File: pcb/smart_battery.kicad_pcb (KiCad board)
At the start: 2 copper layers, 35 parts, among them J11 Conn_01x05_RTC, J12 Conn_HtrTh, J13 Conn_BattTh, Q1 MMBT5551L, Q2 MMBT5551L, U1 SPX3819M5-L-3-3, U10 FEATHER_M0_ADALOGGER, U11 FEATHERWING_HEATER_RELAY, U12 FEATHERWING_ETHERNET, U13 FEATHERWING_MINI_RELAY, U14 FEATHERWING_MINI_RELAY, U1Batt1 LTC4151CS-2PBF, U2Solar1 LTC4151CS-2PBF

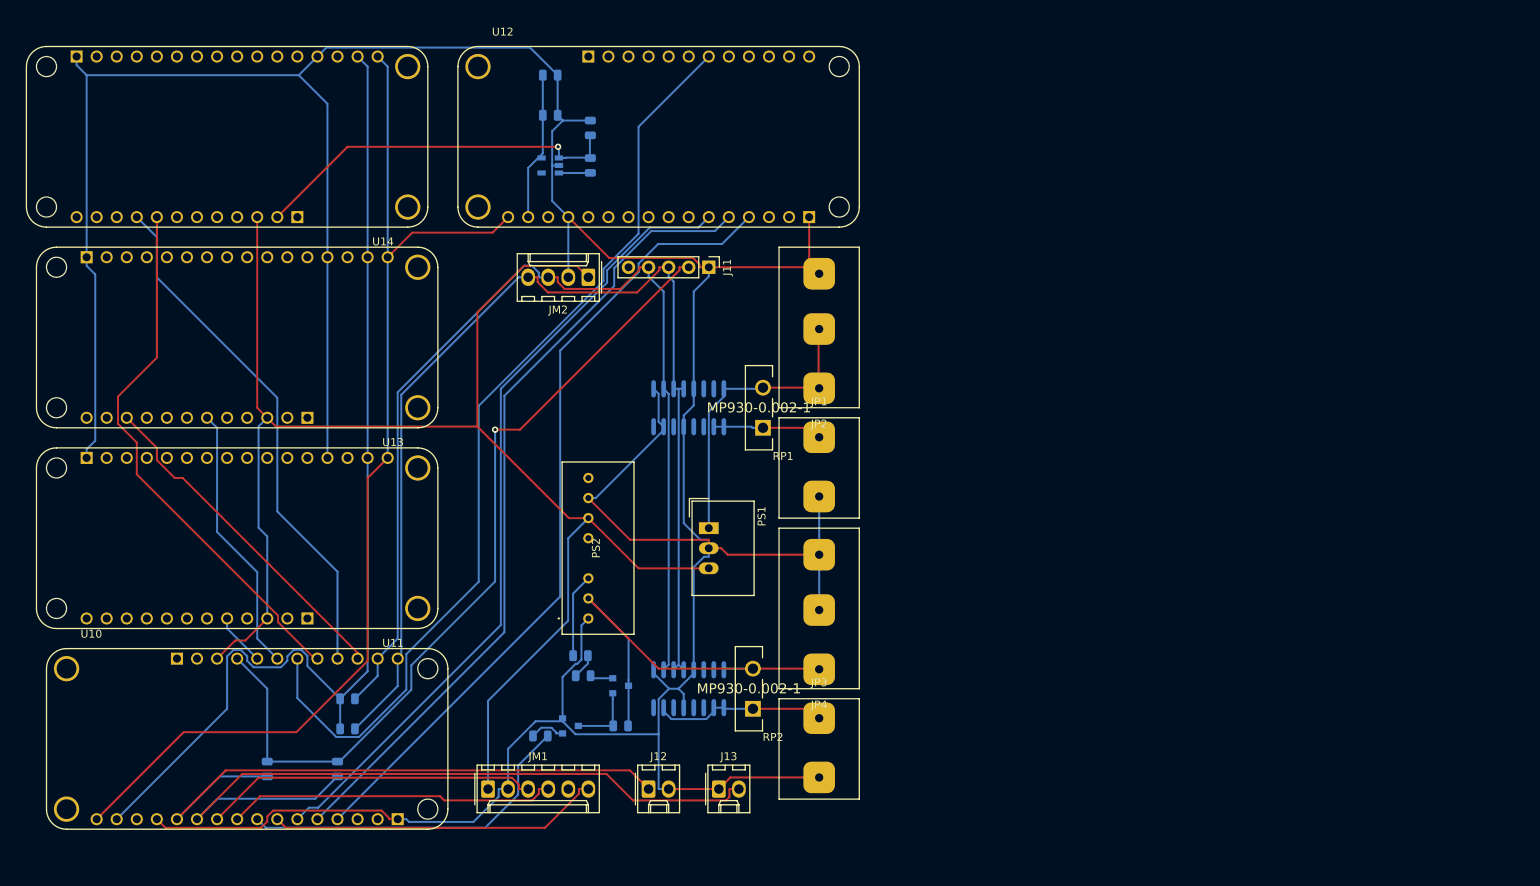
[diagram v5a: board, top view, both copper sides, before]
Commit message: Made gerber files and changed grounds
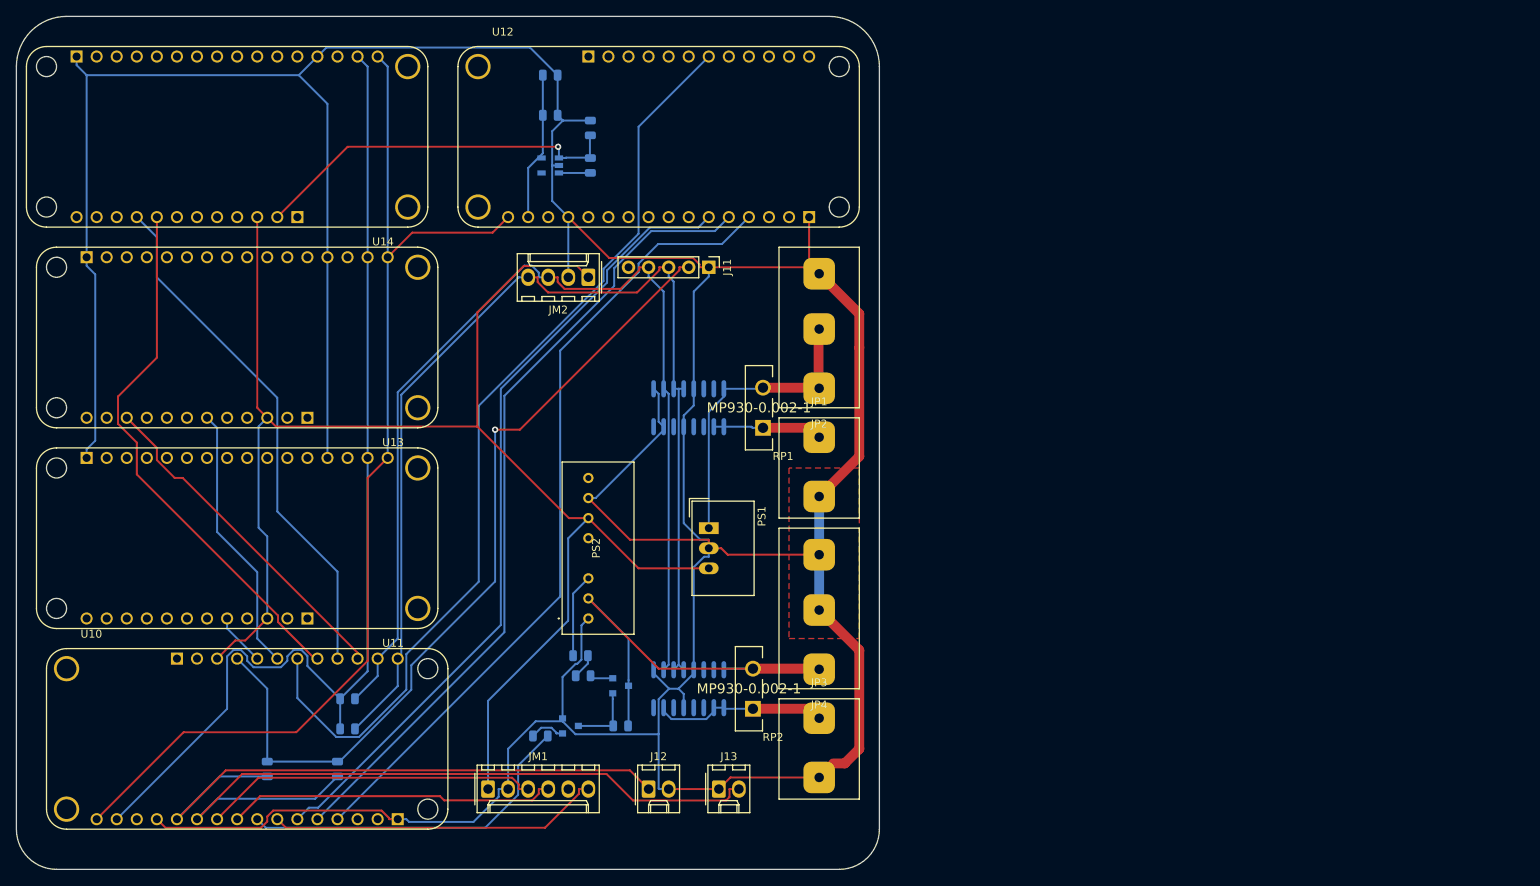
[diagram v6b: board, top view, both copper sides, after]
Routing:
- net GND: track 493.2 -> 551.9 mm
- added copper zone on F.Cu, net GND
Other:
- board outline added: 109.2 x 108 mm
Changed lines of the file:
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@@
   (general
     (thickness 1.6)
-    (drawings 0)
-    (tracks 386)
+    (drawings 8)
+    (tracks 395)
     (zones 0)
     (modules 35)
@@
       (outputformat 1)
       (mirror false)
-      (drillshape 1)
+      (drillshape 0)
       (scaleselection 1)
       (outputdirectory ""))
@@
     (fp_line (start 5.08 2.54) (end 5.08 15.24) (layer F.SilkS) (width 0.15))
     (fp_line (start -5.08 2.54) (end 5.08 2.54) (layer F.SilkS) (width 0.15))
-    (pad 2 thru_hole roundrect (at 0 12.5) (size 4 4) (drill 1.05) (layers *.Cu *.Mask) (roundrect_rratio 0.25)
-      (net 5 GND))
-    (pad 1 thru_hole roundrect (at 0 5) (size 4 4) (drill 1.05) (layers *.Cu *.Mask) (roundrect_rratio 0.25)
+    (pad 2 thru_hole roundrect (at 0 12.5) (size 4 4) (drill 1.2) (layers *.Cu *.Mask) (roundrect_rratio 0.25)
+      (net 5 GND))
+    (pad 1 thru_hole roundrect (at 0 5) (size 4 4) (drill 1.2) (layers *.Cu *.Mask) (roundrect_rratio 0.25)
       (net 4 +24V))
   )
@@
     (fp_line (start 5.08 2.54) (end 5.08 15.24) (layer F.SilkS) (width 0.15))
     (fp_line (start -5.08 2.54) (end 5.08 2.54) (layer F.SilkS) (width 0.15))
-    (pad 2 thru_hole roundrect (at 0 12.5) (size 4 4) (drill 1.05) (layers *.Cu *.Mask) (roundrect_rratio 0.25)
-      (net 5 GND))
-    (pad 1 thru_hole roundrect (at 0 5) (size 4 4) (drill 1.05) (layers *.Cu *.Mask) (roundrect_rratio 0.25)
+    (pad 2 thru_hole roundrect (at 0 12.5) (size 4 4) (drill 1.2) (layers *.Cu *.Mask) (roundrect_rratio 0.25)
+      (net 5 GND))
+    (pad 1 thru_hole roundrect (at 0 5) (size 4 4) (drill 1.2) (layers *.Cu *.Mask) (roundrect_rratio 0.25)
       (net 1 +48V))
   )
@@
     (fp_line (start 5.08 2.54) (end 5.08 22.86) (layer F.SilkS) (width 0.15))
     (fp_line (start -5.08 2.54) (end 5.08 2.54) (layer F.SilkS) (width 0.15))
-    (pad 3 thru_hole roundrect (at 0 19.5 180) (size 4 4) (drill 1.05) (layers *.Cu *.Mask) (roundrect_rratio 0.25)
-      (net 5 GND))
-    (pad 2 thru_hole roundrect (at 0 12.5 180) (size 4 4) (drill 1.05) (layers *.Cu *.Mask) (roundrect_rratio 0.25)
+    (pad 3 thru_hole roundrect (at 0 19.5 180) (size 4 4) (drill 1.2) (layers *.Cu *.Mask) (roundrect_rratio 0.25)
+      (net 5 GND))
+    (pad 2 thru_hole roundrect (at 0 12.5 180) (size 4 4) (drill 1.2) (layers *.Cu *.Mask) (roundrect_rratio 0.25)
       (net 3 /SOLPWR))
-    (pad 1 thru_hole roundrect (at 0 5 180) (size 4 4) (drill 1.05) (layers *.Cu *.Mask) (roundrect_rratio 0.25)
+    (pad 1 thru_hole roundrect (at 0 5 180) (size 4 4) (drill 1.2) (layers *.Cu *.Mask) (roundrect_rratio 0.25)
       (net 3 /SOLPWR))
   )
@@
     (fp_line (start 5.08 2.54) (end 5.08 22.86) (layer F.SilkS) (width 0.15))
     (fp_line (start -5.08 2.54) (end 5.08 2.54) (layer F.SilkS) (width 0.15))
-    (pad 3 thru_hole roundrect (at 0 19.5 180) (size 4 4) (drill 1.05) (layers *.Cu *.Mask) (roundrect_rratio 0.25)
-      (net 5 GND))
-    (pad 2 thru_hole roundrect (at 0 12.5 180) (size 4 4) (drill 1.05) (layers *.Cu *.Mask) (roundrect_rratio 0.25)
-      (net 5 GND))
-    (pad 1 thru_hole roundrect (at 0 5 180) (size 4 4) (drill 1.05) (layers *.Cu *.Mask) (roundrect_rratio 0.25)
+    (pad 3 thru_hole roundrect (at 0 19.5 180) (size 4 4) (drill 1.2) (layers *.Cu *.Mask) (roundrect_rratio 0.25)
+      (net 5 GND))
+    (pad 2 thru_hole roundrect (at 0 12.5 180) (size 4 4) (drill 1.2) (layers *.Cu *.Mask) (roundrect_rratio 0.25)
+      (net 5 GND))
+    (pad 1 thru_hole roundrect (at 0 5 180) (size 4 4) (drill 1.2) (layers *.Cu *.Mask) (roundrect_rratio 0.25)
       (net 2 /BATPWR))
   )
@@
     )
   )
+  (gr_arc (start 27.94 21.59) (end 27.94 15.24) (angle -90) (layer Edge.Cuts) (width 0.15))
+  (gr_arc (start 26.67 118.11) (end 21.59 118.11) (angle -90) (layer Edge.Cuts) (width 0.15))
+  (gr_arc (start 125.73 118.11) (end 125.73 123.19) (angle -90) (layer Edge.Cuts) (width 0.15))
+  (gr_arc (start 124.46 21.59) (end 130.81 21.59) (angle -90) (layer Edge.Cuts) (width 0.15))
+  (gr_line (start 124.46 15.24) (end 27.94 15.24) (layer Edge.Cuts) (width 0.15))
+  (gr_line (start 130.81 118.11) (end 130.81 21.59) (layer Edge.Cuts) (width 0.15))
+  (gr_line (start 26.67 123.19) (end 125.73 123.19) (layer Edge.Cuts) (width 0.15))
+  (gr_line (start 21.59 21.59) (end 21.59 118.11) (layer Edge.Cuts) (width 0.15))
   (segment (start 114.81 102.87) (end 111.265 102.87) (width 0.25) (layer B.Cu) (net 1))
   (segment (start 111.265 102.87) (end 111.125 102.73) (width 0.25) (layer B.Cu) (net 1))
@@
   (segment (start 103.505 103.1808) (end 103.505 102.73) (width 0.25) (layer B.Cu) (net 1))
   (segment (start 109.855 102.73) (end 111.125 102.73) (width 0.25) (layer B.Cu) (net 1))
-  (segment (start 114.81 102.87) (end 122 102.87) (width 0.25) (layer F.Cu) (net 1))
+  (segment (start 114.81 102.87) (end 122 102.87) (width 1.25) (layer F.Cu) (net 1))
   (segment (start 122 102.87) (end 123.19 104.06) (width 0.25) (layer F.Cu) (net 1))
   (segment (start 114.81 97.79) (end 102.87 97.79) (width 0.25) (layer F.Cu) (net 2))
   (segment (start 102.87 97.79) (end 93.98 88.9) (width 0.25) (layer F.Cu) (net 2))
   (segment (start 123.19 97.87) (end 123.11 97.79) (width 0.25) (layer F.Cu) (net 2))
-  (segment (start 123.11 97.79) (end 114.81 97.79) (width 0.25) (layer F.Cu) (net 2))
+  (segment (start 123.11 97.79) (end 114.81 97.79) (width 1.25) (layer F.Cu) (net 2))
   (segment (start 99.0623 99.9575) (end 99.0623 99.2322) (width 0.25) (layer B.Cu) (net 2))
   (segment (start 93.98 88.9) (end 99.0623 93.9823) (width 0.25) (layer B.Cu) (net 2))
@@
   (segment (start 111.265 97.79) (end 111.125 97.93) (width 0.25) (layer B.Cu) (net 2))
   (segment (start 123.11 62.23) (end 123.19 62.31) (width 0.25) (layer F.Cu) (net 3))
-  (segment (start 116.08 62.23) (end 123.11 62.23) (width 0.25) (layer F.Cu) (net 3))
-  (segment (start 123.11 62.23) (end 123.11 54.89) (width 0.25) (layer F.Cu) (net 3))
+  (segment (start 116.08 62.23) (end 123.11 62.23) (width 1.25) (layer F.Cu) (net 3))
+  (segment (start 123.11 62.23) (end 123.11 54.89) (width 1.25) (layer F.Cu) (net 3))
   (segment (start 123.11 54.89) (end 123.19 54.81) (width 0.25) (layer F.Cu) (net 3))
   (segment (start 111.125 62.37) (end 111.125 63.3619) (width 0.25) (layer B.Cu) (net 3))
@@
   (segment (start 114.6147 67.17) (end 114.7547 67.31) (width 0.25) (layer B.Cu) (net 4))
   (segment (start 109.855 67.17) (end 111.125 67.17) (width 0.25) (layer B.Cu) (net 4))
-  (segment (start 116.08 67.31) (end 122 67.31) (width 0.25) (layer F.Cu) (net 4))
+  (segment (start 116.08 67.31) (end 122 67.31) (width 1.25) (layer F.Cu) (net 4))
   (segment (start 122 67.31) (end 123.19 68.5) (width 0.25) (layer F.Cu) (net 4))
   (segment (start 90.7544 28.4207) (end 90.0894 27.7557) (width 0.25) (layer B.Cu) (net 5))
@@
   (segment (start 123.19 83.37) (end 111.6153 83.37) (width 0.25) (layer F.Cu) (net 5))
   (segment (start 111.6153 83.37) (end 110.7953 82.55) (width 0.25) (layer F.Cu) (net 5))
-  (segment (start 123.19 83.37) (end 123.19 76) (width 0.25) (layer B.Cu) (net 5))
-  (segment (start 123.19 90.37) (end 123.19 83.37) (width 0.25) (layer B.Cu) (net 5))
+  (segment (start 123.19 83.37) (end 123.19 76) (width 1.25) (layer B.Cu) (net 5))
+  (segment (start 123.19 90.37) (end 123.19 83.37) (width 1.25) (layer B.Cu) (net 5))
   (segment (start 109.22 46.99) (end 109.22 48.1653) (width 0.25) (layer B.Cu) (net 5))
   (segment (start 107.315 62.37) (end 107.315 50.0703) (width 0.25) (layer B.Cu) (net 5))
   (segment (start 107.315 50.0703) (end 109.22 48.1653) (width 0.25) (layer B.Cu) (net 5))
+  (segment (start 123.19 47.81) (end 128.27 52.89) (width 1.25) (layer F.Cu) (net 5))
+  (segment (start 128.27 52.89) (end 128.27 57.15) (width 1.25) (layer F.Cu) (net 5))
+  (segment (start 128.27 70.92) (end 123.19 76) (width 1.25) (layer F.Cu) (net 5))
+  (segment (start 128.27 57.15) (end 128.27 70.92) (width 1.25) (layer F.Cu) (net 5))
+  (segment (start 124.967817 109.782183) (end 126.437817 109.782183) (width 1.25) (layer F.Cu) (net 5))
+  (segment (start 123.19 111.56) (end 124.967817 109.782183) (width 0.25) (layer F.Cu) (net 5))
+  (segment (start 126.437817 109.782183) (end 128.27 107.95) (width 1.25) (layer F.Cu) (net 5))
+  (segment (start 128.27 95.45) (end 123.19 90.37) (width 1.25) (layer F.Cu) (net 5))
+  (segment (start 128.27 107.95) (end 128.27 95.45) (width 1.25) (layer F.Cu) (net 5))
   (segment (start 88.9 48.26) (end 87.7047 48.26) (width 0.25) (layer B.Cu) (net 6))
   (segment (start 87.7047 48.26) (end 87.7047 47.6624) (width 0.25) (layer B.Cu) (net 6))
@@
   (segment (start 85.1647 112.4324) (end 85.1647 113.03) (width 0.25) (layer F.Cu) (net 137))
   (segment (start 86.36 113.03) (end 85.1647 113.03) (width 0.25) (layer F.Cu) (net 137))
+  (zone (net 5) (net_name GND) (layer F.Cu) (hatch edge 0.508)
+    (connect_pads (clearance 0.508))
+    (min_thickness 0.254)
+    (fill yes (arc_segments 16) (thermal_gap 0.508) (thermal_bridge_width 0.508))
+    (polygon
+      (pts
+        (xy 119.38 72.39) (xy 119.38 93.98) (xy 128.27 93.98) (xy 128.27 72.39)
+      )
+    )
+  )
 )

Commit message: Added mounting holes and Smart Battery label
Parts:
- added REF**: MountingHole_2.5mm, MountingHole:MountingHole_2.5mm, F.Cu at (96.5, 63.5)
- added REF**: MountingHole_2.5mm, MountingHole:MountingHole_2.5mm, F.Cu at (123.2, 118.1)
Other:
- board text added: "Smart Battery https://github.com/Atomicchipmonk"
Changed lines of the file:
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@@
   (general
     (thickness 1.6)
-    (drawings 8)
+    (drawings 9)
     (tracks 395)
     (zones 0)
-    (modules 35)
+    (modules 37)
     (nets 140)
   )
@@
     (mod_text_size 1 1)
     (mod_text_width 0.15)
-    (pad_size 1.524 1.524)
-    (pad_drill 0.762)
+    (pad_size 3.2 3.2)
+    (pad_drill 2.5)
     (pad_to_mask_clearance 0.051)
     (solder_mask_min_width 0.25)
@@
     (add_net "Net-(U2Solar1-Pad8)")
   )
+  (module MountingHole:MountingHole_2.5mm (layer F.Cu)
+    (at 96.52 63.5)
+    (descr "Mounting Hole 2.5mm, no annular")
+    (tags "mounting hole 2.5mm no annular")
+    (attr virtual)
+    (fp_text reference REF** (at 0 -3.5) (layer F.SilkS)
+      (effects (font (size 1 1) (thickness 0.15)))
+    )
+    (fp_text value MountingHole_2.5mm (at 0 3.5) (layer F.Fab)
+      (effects (font (size 1 1) (thickness 0.15)))
+    )
+    (fp_text user %R (at 0.3 0) (layer F.Fab)
+      (effects (font (size 1 1) (thickness 0.15)))
+    )
+    (fp_circle (center 0 0) (end 2.5 0) (layer Cmts.User) (width 0.15))
+    (fp_circle (center 0 0) (end 2.75 0) (layer F.CrtYd) (width 0.05))
+    (pad 1 np_thru_hole circle (at 0 0) (size 2.5 2.5) (drill 2.5) (layers *.Cu *.Mask))
+  )
   (module Connector_Molex:Molex_KK-254_AE-6410-06A_1x06_P2.54mm_Vertical (layer F.Cu)
     (at 81.28 113.03)
@@
     )
   )
+  (module MountingHole:MountingHole_2.5mm (layer F.Cu)
+    (at 123.19 118.11)
+    (descr "Mounting Hole 2.5mm, no annular")
+    (tags "mounting hole 2.5mm no annular")
+    (attr virtual)
+    (fp_text reference REF** (at 0 -3.5) (layer F.SilkS)
+      (effects (font (size 1 1) (thickness 0.15)))
+    )
+    (fp_text value MountingHole_2.5mm (at 0 3.5) (layer F.Fab)
+      (effects (font (size 1 1) (thickness 0.15)))
+    )
+    (fp_circle (center 0 0) (end 2.75 0) (layer F.CrtYd) (width 0.05))
+    (fp_circle (center 0 0) (end 2.5 0) (layer Cmts.User) (width 0.15))
+    (fp_text user %R (at 0.3 0) (layer F.Fab)
+      (effects (font (size 1 1) (thickness 0.15)))
+    )
+    (pad 1 np_thru_hole circle (at 0 0) (size 2.5 2.5) (drill 2.5) (layers *.Cu *.Mask))
+  )
+  (gr_text "Smart Battery https://github.com/Atomicchipmonk\n" (at 85.09 120.65) (layer F.Cu)
+    (effects (font (size 1.5 1.5) (thickness 0.3)))
+  )
   (gr_arc (start 27.94 21.59) (end 27.94 15.24) (angle -90) (layer Edge.Cuts) (width 0.15))

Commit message: Added diodes to protect battery inputs
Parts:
- removed REF** (x2): MountingHole_2.5mm, MountingHole:MountingHole_2.5mm
- added D1: 1N4002, Diode_THT:D_DO-41_SOD81_P10.16mm_Horizontal, F.Cu at (86.4, 87.6)
- added D2: 1N4001, Diode_THT:D_DO-41_SOD81_P10.16mm_Horizontal, F.Cu at (97.8, 68.6)
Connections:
- PS1 pad 1: /SOLPWR -> Net-(D2-Pad1)
- PS2 pad 2: /BATPWR -> /DBPWR
- Q1 pad 3: /BATPWR -> /DBPWR
- R6 pad 1: /BATPWR -> /DBPWR
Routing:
- net /DBPWR: track 0.00 -> 27.2 mm
- net Net-(D2-Pad1): track 0.00 -> 16.2 mm
- net /BATPWR: track 54.9 -> 49.0 mm
- net /SOLPWR: track 38.0 -> 43.2 mm
